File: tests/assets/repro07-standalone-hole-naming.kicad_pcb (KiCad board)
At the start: 2 copper layers, 20 x 20 mm, 2 parts

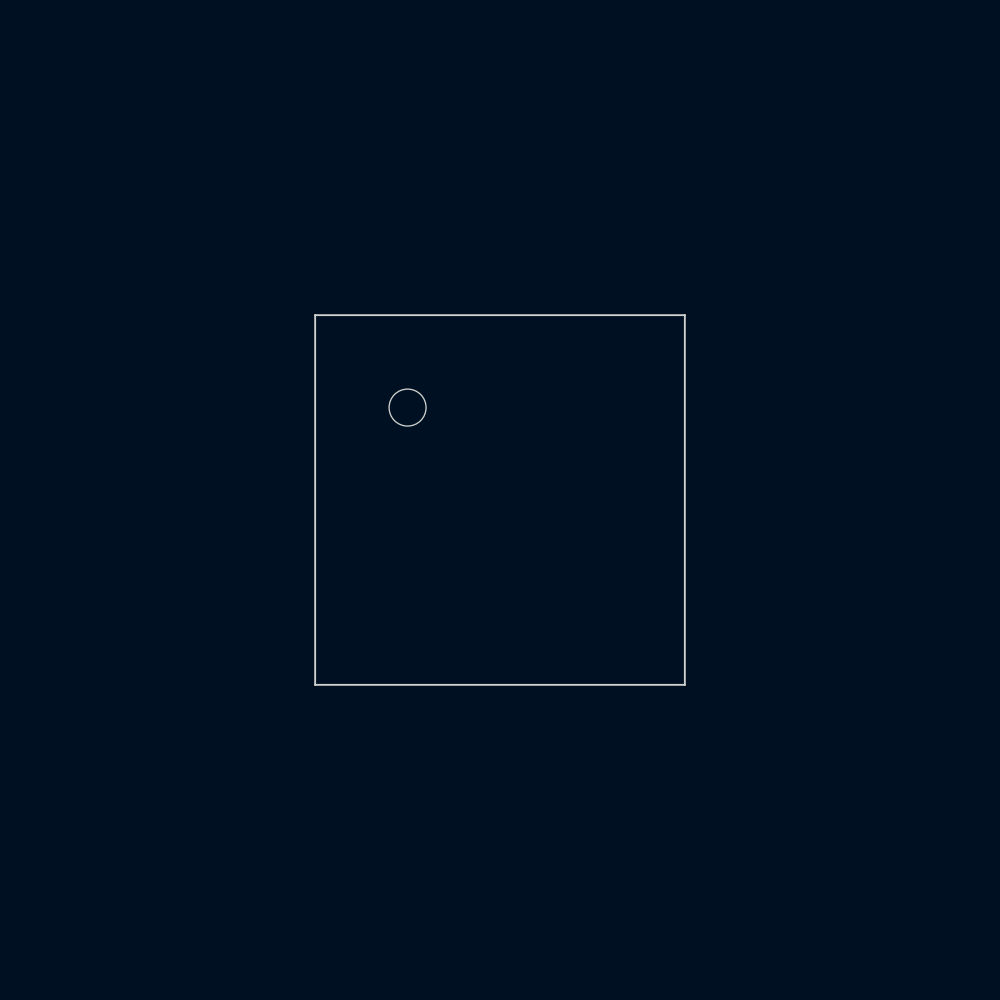
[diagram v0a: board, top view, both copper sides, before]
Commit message: feat: Dynamically name standalone PCB hole footprints in KiCad based on their shape and dimensions
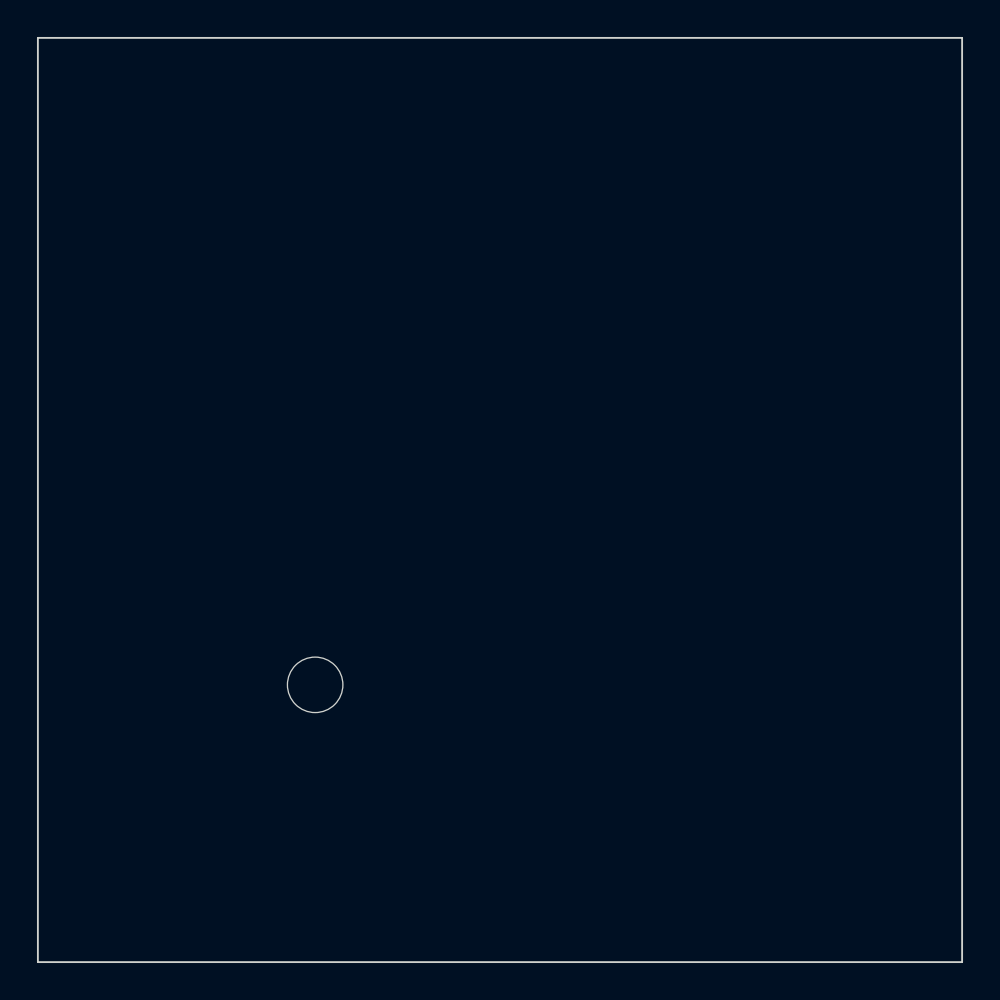
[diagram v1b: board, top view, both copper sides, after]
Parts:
- removed the ? at (100.0, 100.0) (x2)
- added ?: , tscircuit:hole_circle_3mm, F.Cu at (100.0, 100.0)
- added ?: , tscircuit:hole_pill_4mm_2mm, F.Cu at (100.0, 100.0)
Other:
- board size 20 x 20 mm -> 50 x 50 mm
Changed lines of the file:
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@@
   (net 0 "")
   (footprint
-    "tscircuit:hole_circle_2mm"
+    "tscircuit:hole_circle_3mm"
     (layer F.Cu)
     (at 100 100 0)
     (pad "" np_thru_hole circle
-      (at -5 -5 0)
-      (size 2 2)
-      (drill 2)
+      (at -10 10 0)
+      (size 3 3)
+      (drill 3)
       (layers *.Cu *.Mask)
     )
   )
   (footprint
-    "tscircuit:hole_pill_2mm_4mm"
+    "tscircuit:hole_pill_4mm_2mm"
     (layer F.Cu)
     (at 100 100 0)
     (pad "" np_thru_hole oval
-      (at 5 -5 0)
-      (size 2 4)
-      (drill oval 2 4)
+      (at 10 -10 0)
+      (size 4 2)
+      (drill oval 4 2)
       (layers *.Cu *.Mask)
     )
   )
   (gr_line
-    (start 90 110)
-    (end 110 110)
+    (start 75 125)
+    (end 125 125)
     (width 0.1)
     (layer Edge.Cuts)
   )
   (gr_line
-    (start 110 110)
-    (end 110 90)
+    (start 125 125)
+    (end 125 75)
     (width 0.1)
     (layer Edge.Cuts)
   )
   (gr_line
-    (start 110 90)
-    (end 90 90)
+    (start 125 75)
+    (end 75 75)
     (width 0.1)
     (layer Edge.Cuts)
   )
   (gr_line
-    (start 90 90)
-    (end 90 110)
+    (start 75 75)
+    (end 75 125)
     (width 0.1)
     (layer Edge.Cuts)
